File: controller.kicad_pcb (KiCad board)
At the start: 2 copper layers, 29.2 x 36.2 mm, 27 parts, among them J1 Conn_ST_STDC14, J2 USB_C_Receptacle_USB2.0_14P, SW1 SW_Push, SW2 SW_Push, U1 STM32L476RGTx, U2 BD33FC0FP, U3 NUP2202

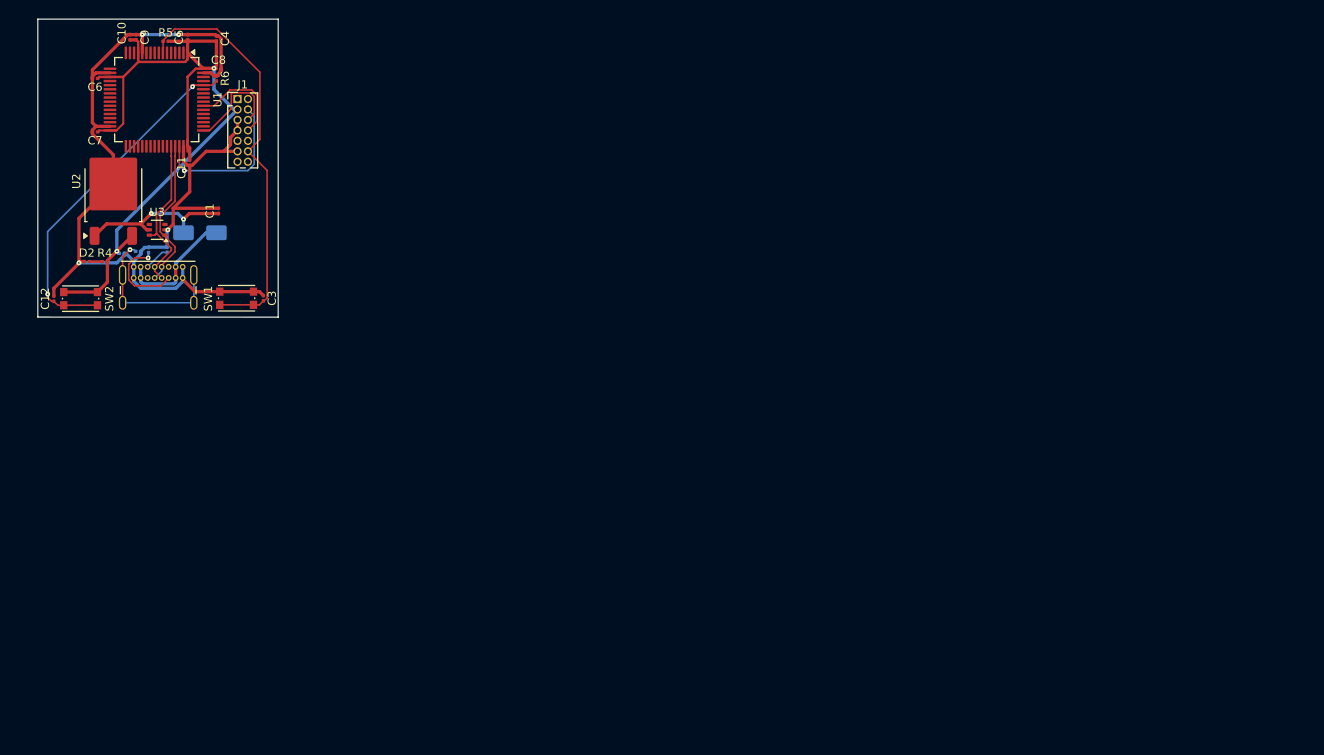
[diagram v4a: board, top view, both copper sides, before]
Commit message: add some control components to schematic and pcb
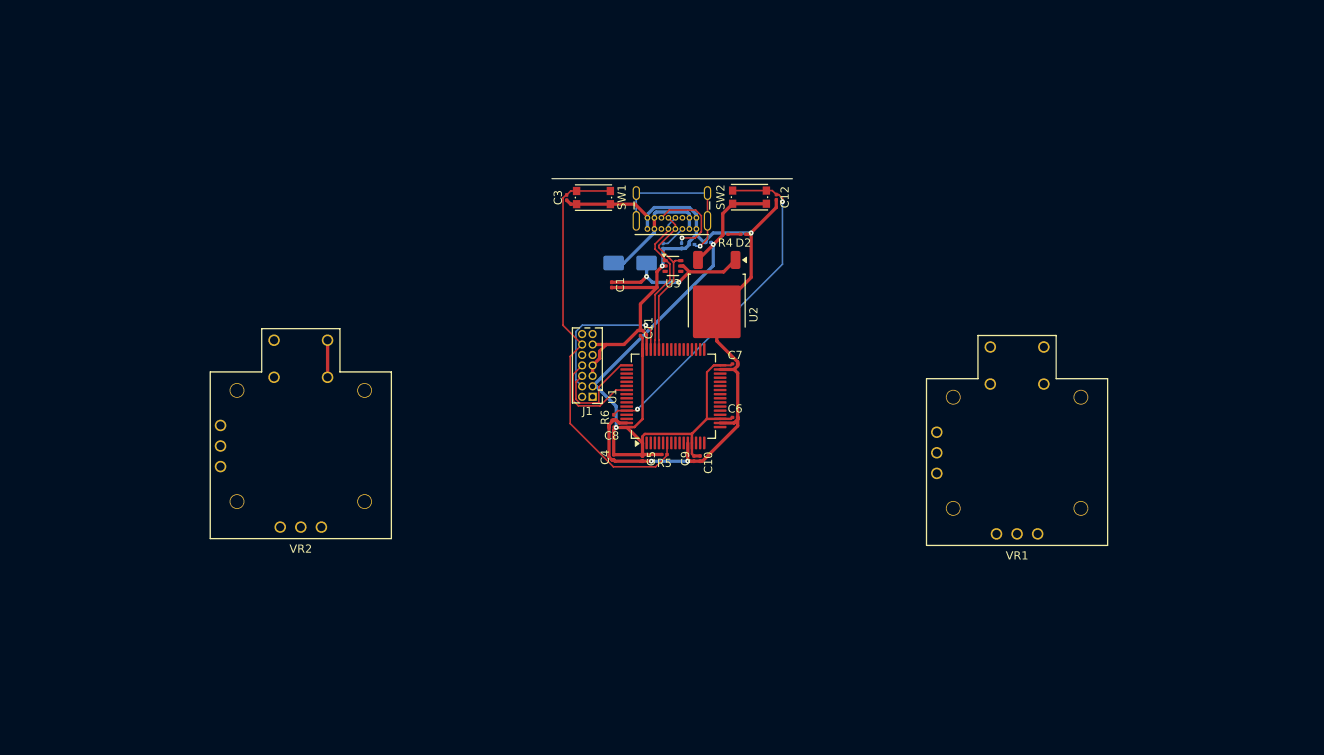
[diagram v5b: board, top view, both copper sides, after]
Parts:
- added VR1: ~, 3D16A1N:3D16A1N, F.Cu at (180.7, 98.5)
- added VR2: ~, 3D16A1N:3D16A1N, F.Cu at (93.7, 97.6)
- moved C12 88.6 mm to (151.5, 67.4), turned to -90 degrees
- moved C6 88.0 mm to (146.5, 94.2), turned to 0 degrees
- moved C10 86.1 mm to (142.2, 99.2), turned to 90 degrees
- moved C9 84.9 mm to (141.5, 99.2), turned to 90 degrees
- moved C7 82.7 mm to (146.5, 87.7), turned to 0 degrees
- moved SW2 82.2 mm to (148.2, 67.4), turned to 180 degrees
- moved D2 79.8 mm to (147.5, 71.9), turned to 180 degrees
- moved R5 78.7 mm to (137.9, 98.7), turned to 180 degrees
- moved R4 75.5 mm to (145.3, 71.9), turned to 0 degrees
- moved C5 75.3 mm to (135.3, 99.2), turned to -90 degrees
- moved U2 74.4 mm to (144.3, 80.1), turned to -90 degrees
- moved U1 72.4 mm to (139.0, 91.6), turned to 90 degrees
- moved C2 71.3 mm to (143.2, 72.9), turned to 0 degrees
- moved C4 70.1 mm to (131.8, 99.0), turned to 90 degrees
- moved J2 68.5 mm to (141.8, 71.3), turned to 180 degrees
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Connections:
- U1 pad 24: unconnected-(U1-PC4-Pad24) -> RightClick
- U1 pad 25: unconnected-(U1-PC5-Pad25) -> LeftClick
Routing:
- net +3.3V: track 96.7 -> 101.2 mm
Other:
- board outline removed

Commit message: finish routing, more or less
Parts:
- added R10: 10k, Resistor_SMD:R_0201_0603Metric, F.Cu at (138.9, 102.6)
- added R11: 10k, Resistor_SMD:R_0201_0603Metric, B.Cu at (127.4, 96.3)
- added R12: 10k, Resistor_SMD:R_0201_0603Metric, B.Cu at (128.2, 97.2)
- added R13: 10k, Resistor_SMD:R_0201_0603Metric, F.Cu at (144.0, 96.7)
- added R14: 10k, Resistor_SMD:R_0201_0603Metric, F.Cu at (144.8, 95.7)
- added R7: 10k, Resistor_SMD:R_0201_0603Metric, F.Cu at (138.9, 101.2)
- added R8: 10k, Resistor_SMD:R_0201_0603Metric, F.Cu at (167.1, 85.7)
- added R9: 10k, Resistor_SMD:R_0201_0603Metric, F.Cu at (167.1, 83.8)
- added SW10: SW_Push, Button_Switch_SMD:SW_Push_1P1T-MP_NO_Horizontal_Alps_SKRTLAE010, F.Cu at (194.8, 64.5)
- added SW11: SW_Push, Button_Switch_SMD:SW_Push_1P1T-MP_NO_Horizontal_Alps_SKRTLAE010, B.Cu at (188.6, 64.5)
- added SW3: SW_Push, Button_Switch_SMD:SW_Push_1P1T_NO_CK_PTS125Sx43SMTR, F.Cu at (179.9, 94.8)
- added SW4: SW_Push, Button_Switch_SMD:SW_Push_1P1T_NO_CK_PTS125Sx43SMTR, F.Cu at (193.3, 81.6)
- added SW5: SW_Push, Button_Switch_SMD:SW_Push_1P1T_NO_CK_PTS125Sx43SMTR, F.Cu at (206.2, 94.8)
- added SW6: SW_Push, Button_Switch_SMD:SW_Push_1P1T_NO_CK_PTS125Sx43SMTR, F.Cu at (193.3, 107.9)
- added SW7: ~, K1-1210UN-01:K1-1210UN-01, F.Cu at (82.5, 94.7)
- added SW8: SW_Push, Button_Switch_SMD:SW_Push_1P1T-MP_NO_Horizontal_Alps_SKRTLAE010, F.Cu at (80.4, 64.5)
- added SW9: SW_Push, Button_Switch_SMD:SW_Push_1P1T-MP_NO_Horizontal_Alps_SKRTLAE010, B.Cu at (85.9, 64.5)
- SW1, SW2: moved to B.Cu
- moved VR2 26.7 mm to (108.8, 119.6)
- moved VR1 26.0 mm to (165.7, 119.6)
- moved R2 5.68 mm to (137.3, 68.3)
- moved C12 2.71 mm to (148.8, 67.2)
- moved C1 1.55 mm to (129.9, 78.1)
- moved C10 1.55 mm to (140.7, 99.2)
- moved C11 1.55 mm to (133.4, 83.9)
- moved C2 1.55 mm to (141.7, 72.9)
- moved C4 1.55 mm to (130.2, 99.0)
- moved C5 1.55 mm to (133.7, 99.2)
- moved C6 1.55 mm to (144.9, 94.2)
- moved C7 1.55 mm to (144.9, 87.7)
- moved C8 1.55 mm to (130.0, 95.4)
- moved C9 1.55 mm to (139.9, 99.2)
- moved D1 1.55 mm to (132.2, 75.4)
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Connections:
- U1 pad 10: LeftX -> RightX
- U1 pad 11: LeftY -> RightY
- U1 pad 14: unconnected-(U1-PA0-Pad14) -> LeftTriggerTop
- U1 pad 15: unconnected-(U1-PA1-Pad15) -> LeftTriggerBottom
- U1 pad 16: unconnected-(U1-PA2-Pad16) -> RightTriggerTop
- U1 pad 17: unconnected-(U1-PA3-Pad17) -> RightTriggerBottom
- U1 pad 2: unconnected-(U1-PC13-Pad2) -> ButtonDown
- U1 pad 20: unconnected-(U1-PA4-Pad20) -> SelectINS
- U1 pad 21: unconnected-(U1-PA5-Pad21) -> SPI1_SCK
- U1 pad 22: unconnected-(U1-PA6-Pad22) -> SPI1_MISO
- U1 pad 23: unconnected-(U1-PA7-Pad23) -> SPI1_MOSI
- U1 pad 3: unconnected-(U1-PC14-Pad3) -> ButtonLeft
- U1 pad 37: unconnected-(U1-PC6-Pad37) -> DPadUp
- U1 pad 38: unconnected-(U1-PC7-Pad38) -> DPadRight
- U1 pad 39: unconnected-(U1-PC8-Pad39) -> DPadDown
- U1 pad 40: unconnected-(U1-PC9-Pad40) -> DPadLeft
- U1 pad 51: unconnected-(U1-PC10-Pad51) -> DPadCenter
- U1 pad 52: unconnected-(U1-PC11-Pad52) -> ButtonUp
- U1 pad 53: unconnected-(U1-PC12-Pad53) -> ButtonRight
- U1 pad 8: RightX -> LeftX
- U1 pad 9: RightY -> LeftY
- VR1 pad 3: Net-(VR1-VSS) -> GND
- VR1 pad 3': Net-(VR1-VSS') -> GND
- VR2 pad 3: Net-(VR2-VSS) -> GND
- VR2 pad 3': Net-(VR2-VSS') -> GND
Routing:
- net +3.3V: track 101.2 -> 547.4 mm, vias 2 -> 5
- net GND: track 128.4 -> 269.3 mm, vias 4 -> 7
- net ButtonRight: track 0.00 -> 99.6 mm, vias 0 -> 2
- net LeftTriggerTop: track 0.00 -> 78.7 mm, vias 0 -> 2
- net ButtonUp: track 0.00 -> 76.9 mm, vias 0 -> 2
- net LeftTriggerBottom: track 0.00 -> 74.7 mm, vias 0 -> 1
- net DPadLeft: track 0.00 -> 73.2 mm, vias 0 -> 2
- net ButtonLeft: track 0.00 -> 71.9 mm, vias 0 -> 2
- net DPadDown: track 0.00 -> 71.9 mm, vias 0 -> 2
- net RightX: track 0.00 -> 70.9 mm, vias 0 -> 2
- net RightTriggerTop: track 0.00 -> 67.3 mm, vias 0 -> 2
- net ButtonDown: track 0.00 -> 66.0 mm, vias 0 -> 1
- net DPadUp: track 0.00 -> 65.5 mm, vias 0 -> 2
- net DPadRight: track 0.00 -> 63.4 mm, vias 0 -> 2
- net RightTriggerBottom: track 0.00 -> 62.6 mm, vias 0 -> 1
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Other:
- board outline added: 156.8 x 70.7 mm
- board text added: "RESET"

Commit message: fix most drc issues
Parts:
- moved R14 0.10 mm to (144.9, 95.7)
- turned SW7 to -45 degrees
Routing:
- net +3.3V: track 547.4 -> 566.1 mm, vias 5 -> 6
- net ButtonDown: track 66.0 -> 76.8 mm, vias 1 -> 2
- net LeftY: track 51.3 -> 54.8 mm
- net DPadLeft: track 73.2 -> 74.6 mm
- net DPadDown: track 71.9 -> 73.2 mm
- net DPadCenter: track 49.7 -> 50.7 mm
- net LeftX: track 51.3 -> 50.3 mm
- net GND: track 269.3 -> 270.2 mm
- net ButtonLeft: track 71.9 -> 71.4 mm

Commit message: add vanity
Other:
- board text added: "https://github.com/CodeTriangle/kicad-gamepad"
